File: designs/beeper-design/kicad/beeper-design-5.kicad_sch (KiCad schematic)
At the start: 7 parts, among them U12 DRV2605YZFR

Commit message: new export
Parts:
- removed C47: 2.2u, beeper-design:Pkg0201_11, symbol C335106_9
- removed C48: 2.2u, beeper-design:Pkg0201_24, symbol C335106_17
- removed R16, R17: 8K2, beeper-design:Pkg0201_39, symbol my_resistor_9
- added C47: 2.2u, beeper-design:Pkg0201_4, symbol C335106_2
- added C48: 2.2u, beeper-design:Pkg0201_16, symbol C335106_10
- added R16, R17: 8K2, beeper-design:Pkg0201_31, symbol my_resistor_8
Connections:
- net GND: now also C47.1, C48.1
- net VDDSYS: now also C48.2, R16.2, R17.2
- net mcu_hap-i2c_scl: now also R17.1
- net mcu_hap-i2c_sda: now also R16.1
- net at U12.A2 (REG): now also C47.2

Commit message: reasonble export
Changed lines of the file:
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@@
   (wire (pts (xy 248.92 113.03) (xy 248.92 111.76)) (stroke (width 0.127) (type default) (color 0 0 0 0)))
   (wire (pts (xy 228.6 121.92) (xy 233.68 121.92)) (stroke (width 0.127) (type default) (color 0 0 0 0)))
-  (wire (pts (xy 229.87 121.92) (xy 229.87 119.38)) (stroke (width 0.127) (type default) (color 0 0 0 0)))
+  (wire (pts (xy 231.14 121.92) (xy 231.14 120.65)) (stroke (width 0.127) (type default) (color 0 0 0 0)))
   (wire (pts (xy 264.16 116.84) (xy 264.16 115.57)) (stroke (width 0.127) (type default) (color 0 0 0 0)))
   (wire (pts (xy 247.65 139.7) (xy 247.65 138.43)) (stroke (width 0.127) (type default) (color 0 0 0 0)))
@@
 (junction (at 181.61 127.0) (diameter 0.762) (color 0 0 0 0 ))
 (junction (at 213.36 124.46) (diameter 0.762) (color 0 0 0 0 ))
-(junction (at 229.87 121.92) (diameter 0.762) (color 0 0 0 0 ))
+(junction (at 231.14 121.92) (diameter 0.762) (color 0 0 0 0 ))
   (label "board-io_hapdrv" (at 151.13 100.33 0)
     (effects (font (size 0.762 0.762)) (justify left bottom ))
@@
     (effects (font (size 0.762 0.762)) (justify left ))
   )
-  (global_label "mcu_hap-gpio0_gpio" (shape passive) (at 229.87 119.38 90)
+  (global_label "mcu_hap-gpio0_gpio" (shape passive) (at 231.14 120.65 90)
     (effects (font (size 0.762 0.762)) (justify left ))
   )
@@
     (instances
       (project "beeper-design"
-        (path "/219df102-d28d-b743-245e-efc9439ef913"
+        (path "/de0561a0-459a-4fb5-54e5-6d5ccc441e19"
           (reference "C48") (unit 1)
         )
@@
     (instances
       (project "beeper-design"
-        (path "/219df102-d28d-b743-245e-efc9439ef913"
+        (path "/de0561a0-459a-4fb5-54e5-6d5ccc441e19"
           (reference "R16") (unit 1)
         )
@@
     (instances
       (project "beeper-design"
-        (path "/219df102-d28d-b743-245e-efc9439ef913"
+        (path "/de0561a0-459a-4fb5-54e5-6d5ccc441e19"
           (reference "TP2") (unit 1)
         )
@@
     (instances
       (project "beeper-design"
-        (path "/219df102-d28d-b743-245e-efc9439ef913"
+        (path "/de0561a0-459a-4fb5-54e5-6d5ccc441e19"
           (reference "TP1") (unit 1)
         )
@@
     (instances
       (project "beeper-design"
-        (path "/219df102-d28d-b743-245e-efc9439ef913"
+        (path "/de0561a0-459a-4fb5-54e5-6d5ccc441e19"
           (reference "R17") (unit 1)
         )
@@
     (instances
       (project "beeper-design"
-        (path "/219df102-d28d-b743-245e-efc9439ef913"
+        (path "/de0561a0-459a-4fb5-54e5-6d5ccc441e19"
           (reference "U12") (unit 1)
         )
@@
     (instances
       (project "beeper-design"
-        (path "/219df102-d28d-b743-245e-efc9439ef913"
+        (path "/de0561a0-459a-4fb5-54e5-6d5ccc441e19"
           (reference "C47") (unit 1)
         )
@@
     (instances
       (project "beeper-design"
-        (path "/219df102-d28d-b743-245e-efc9439ef913"
+        (path "/de0561a0-459a-4fb5-54e5-6d5ccc441e19"
           (reference "#PWR?") (unit 1)
         )
@@
     (instances
       (project "beeper-design"
-        (path "/219df102-d28d-b743-245e-efc9439ef913"
+        (path "/de0561a0-459a-4fb5-54e5-6d5ccc441e19"
           (reference "#PWR?") (unit 1)
         )
@@
     (instances
       (project "beeper-design"
-        (path "/219df102-d28d-b743-245e-efc9439ef913"
+        (path "/de0561a0-459a-4fb5-54e5-6d5ccc441e19"
           (reference "#PWR?") (unit 1)
         )
@@
     (instances
       (project "beeper-design"
-        (path "/219df102-d28d-b743-245e-efc9439ef913"
+        (path "/de0561a0-459a-4fb5-54e5-6d5ccc441e19"
           (reference "#PWR?") (unit 1)
         )
@@
     (instances
       (project "beeper-design"
-        (path "/219df102-d28d-b743-245e-efc9439ef913"
+        (path "/de0561a0-459a-4fb5-54e5-6d5ccc441e19"
           (reference "#PWR?") (unit 1)
         )
@@
     (instances
       (project "beeper-design"
-        (path "/219df102-d28d-b743-245e-efc9439ef913"
+        (path "/de0561a0-459a-4fb5-54e5-6d5ccc441e19"
           (reference "#PWR?") (unit 1)
         )
@@
     (instances
       (project "beeper-design"
-        (path "/219df102-d28d-b743-245e-efc9439ef913"
-          (reference "#PWR?") (unit 1)
-        )
+        (path "/de0561a0-459a-4fb5-54e5-6d5ccc441e19"
+          (reference "#PWR?") (unit 1)
+        )

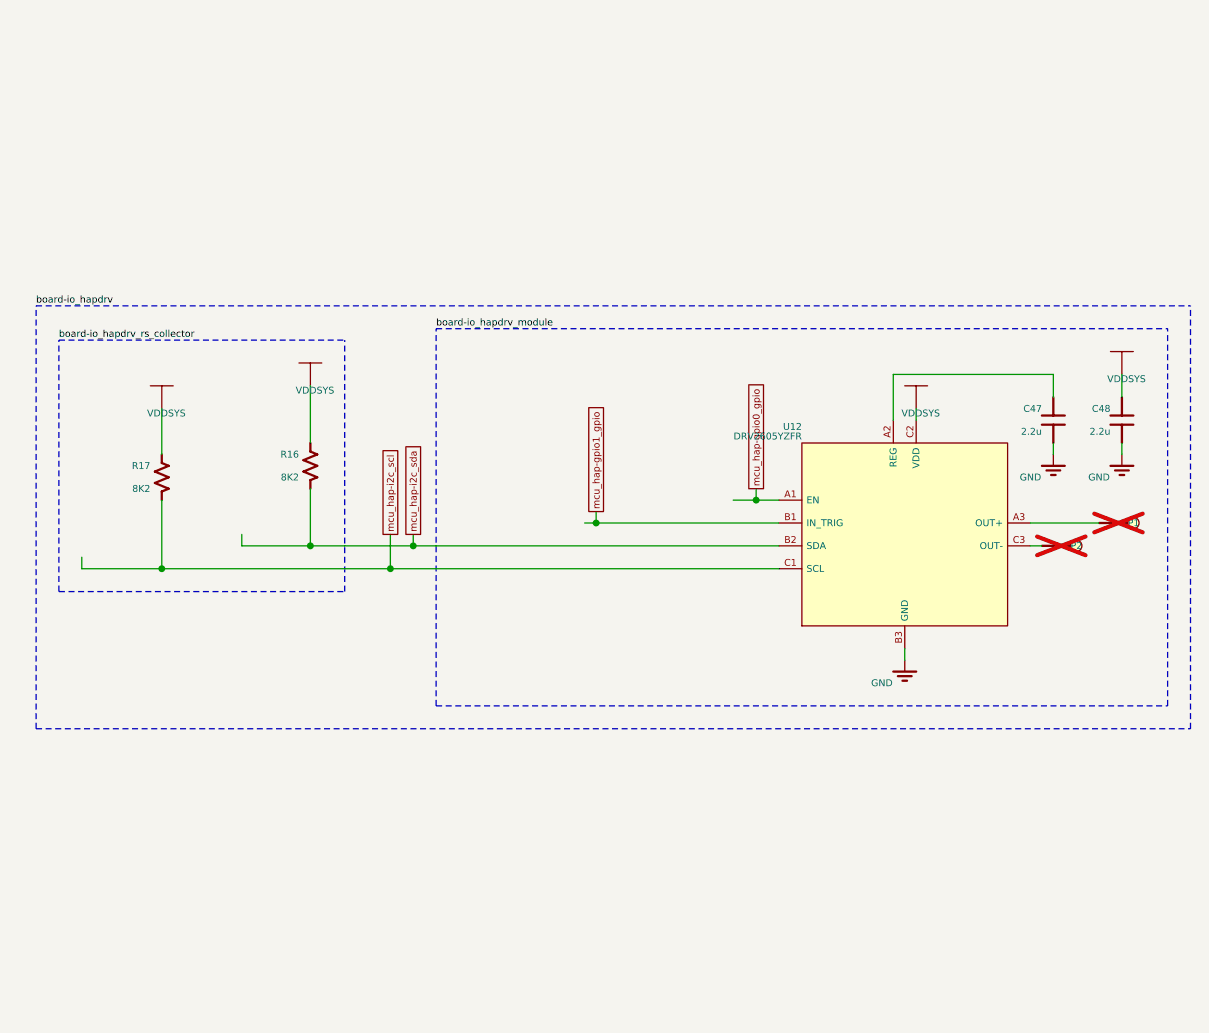
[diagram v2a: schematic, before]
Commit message: exported, yet XTALM32p keeps disappearing
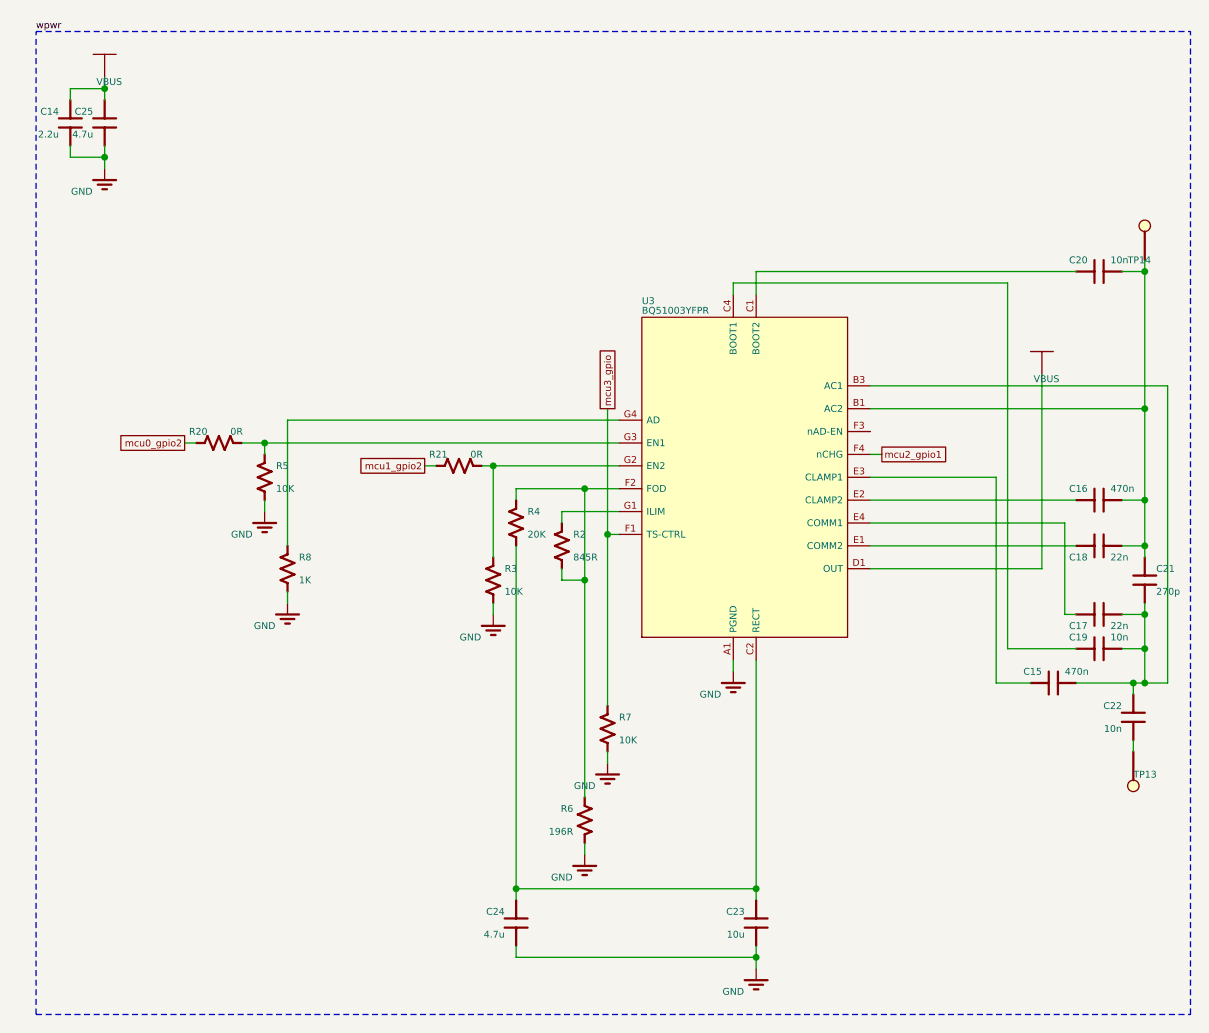
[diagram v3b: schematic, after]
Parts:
- removed C47: 2.2u, beeper-design:Pkg0201_4, symbol C335106_2
- removed C48: 2.2u, beeper-design:Pkg0201_16, symbol C335106_10
- removed R16, R17: 8K2, beeper-design:Pkg0201_31, symbol my_resistor_8
- removed TP1, TP2: (no value), beeper-design:SMD_TESTPT, symbol smd_testpoint_cmp
- removed U12: DRV2605YZFR, beeper-design:LP_7, symbol DRV2605YZFR
- added C14: 2.2u, beeper-design:Pkg0201_20, symbol C335106
- added C15: 470n, beeper-design:Pkg0201_23, symbol my_capacitor_12
- added C16: 470n, beeper-design:Pkg0201_30, symbol my_capacitor_16
- added C17: 22n, beeper-design:Pkg0201_36, symbol C505472
- added C18: 22n, beeper-design:Pkg0201_44, symbol C505472_1
- added C19: 10n, beeper-design:Pkg0201_2, symbol my_capacitor_2
- added C20: 10n, beeper-design:Pkg0201_11, symbol my_capacitor_6
- added C21: 270p, beeper-design:Pkg0201_17, symbol my_capacitor_9
- added C22: 10n, beeper-design:Pkg0201_22, symbol my_capacitor_11
- added C23: 10u, beeper-design:Pkg0402_4, symbol C105225_3
- added C24: 4.7u, beeper-design:Pkg0402_7, symbol C23733
- added C25: 4.7u, beeper-design:Pkg0402_8, symbol C23733_1
- added R2: 845R, beeper-design:Pkg0201_25, symbol my_resistor_10
- added R20: 0R, beeper-design:Pkg0201, symbol my_resistor
- added R21: 0R, beeper-design:Pkg0201_8, symbol my_resistor_3
- added R3: 10K, beeper-design:Pkg0201_4, symbol my_resistor_2
- added R4: 20K, beeper-design:Pkg0201_37, symbol my_resistor_12
- added R5: 10K, beeper-design:Pkg0201_45, symbol my_resistor_15
- added R6: 196R, beeper-design:Pkg0201_32, symbol C138167
- added R7: 10K, beeper-design:Pkg0201_12, symbol my_resistor_6
- added R8: 1K, beeper-design:Pkg0201_16, symbol my_resistor_8
- added TP13, TP14: (no value), beeper-design:SMD_TESTPT, symbol smd_testpoint_cmp
- added U3: BQ51003YFPR, beeper-design:LP_6, symbol BQ51003YFPR
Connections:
- net GND: now also C14.1, C23.1, C24.1, C25.1, R3.2, R5.2, R6.2, R7.2, R8.2, U3.A1 (PGND), U3.A2 (PGND), U3.A3 (PGND), U3.A4 (PGND)
- new net: C15.1, C17.1, C19.1, C21.2, C22.2, U3.B3 (AC1), U3.B4 (AC1)
- new net: C15.2, U3.E3 (CLAMP1)
- new net: R21.1, R3.1, U3.G2 (EN2)
- new net: R2.2, R4.1, R6.1, U3.F2 (FOD)
- new net: C23.2, C24.2, R4.2, U3.C2 (RECT), U3.C3 (RECT)
- new net: C16.1, C18.1, C20.1, C21.1, TP14.p, U3.B1 (AC2), U3.B2 (AC2)
- new net: C20.2, U3.C1 (BOOT2)
- new net: C19.2, U3.C4 (BOOT1)
- new net: C16.2, U3.E2 (CLAMP2)
- new net: C17.2, U3.E4 (COMM1)
- new net: R20.1, R5.1, U3.G3 (EN1)
- new net: C18.2, U3.E1 (COMM2)
- new net: R2.1, U3.G1 (ILIM)
- new net: R8.1, U3.G4 (AD)
- new net: C22.1, TP13.p
- new net VBUS: C14.2, C25.2, U3.D1 (OUT), U3.D2 (OUT), U3.D3 (OUT), U3.D4 (OUT)
- new net mcu0_gpio2: R20.2
- new net mcu1_gpio2: R21.2
- new net mcu2_gpio1: U3.F4 (nCHG)
- new net mcu3_gpio: R7.1, U3.F1 (TS-CTRL)

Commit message: fixed up pours, keepout regions
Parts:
- removed C15: 470n, beeper-design:Pkg0201_23, symbol my_capacitor_12
- removed C16: 470n, beeper-design:Pkg0201_30, symbol my_capacitor_16
- removed C19: 10n, beeper-design:Pkg0201_2, symbol my_capacitor_2
- removed C20: 10n, beeper-design:Pkg0201_11, symbol my_capacitor_6
- removed C21: 270p, beeper-design:Pkg0201_17, symbol my_capacitor_9
- removed C22: 10n, beeper-design:Pkg0201_22, symbol my_capacitor_11
- removed C24: 4.7u, beeper-design:Pkg0402_7, symbol C23733
- removed C25: 4.7u, beeper-design:Pkg0402_8, symbol C23733_1
- removed R2: 845R, beeper-design:Pkg0201_25, symbol my_resistor_10
- removed R20: 0R, beeper-design:Pkg0201, symbol my_resistor
- removed R21: 0R, beeper-design:Pkg0201_8, symbol my_resistor_3
- removed R3: 10K, beeper-design:Pkg0201_4, symbol my_resistor_2
- removed R4: 20K, beeper-design:Pkg0201_37, symbol my_resistor_12
- removed R5: 10K, beeper-design:Pkg0201_45, symbol my_resistor_15
- removed R7: 10K, beeper-design:Pkg0201_12, symbol my_resistor_6
- removed R8: 1K, beeper-design:Pkg0201_16, symbol my_resistor_8
- added C15: 470n, beeper-design:Pkg0201_37, symbol my_capacitor_18
- added C16: 470n, beeper-design:Pkg0201_44, symbol my_capacitor_22
- added C19: 10n, beeper-design:Pkg0201_16, symbol my_capacitor_8
- added C20: 10n, beeper-design:Pkg0201_25, symbol my_capacitor_12
- added C21: 270p, beeper-design:Pkg0201_31, symbol my_capacitor_15
- added C22: 10n, beeper-design:Pkg0201_36, symbol my_capacitor_17
- added C24: 4.7u, beeper-design:Pkg0402, symbol C23733_1
- added C25: 4.7u, beeper-design:Pkg0402_1, symbol C23733
- added R2: 845R, beeper-design:Pkg0201_39, symbol my_resistor_15
- added R20: 0R, beeper-design:Pkg0201_14, symbol my_resistor_5
- added R21: 0R, beeper-design:Pkg0201_22, symbol my_resistor_8
- added R3: 10K, beeper-design:Pkg0201_18, symbol my_resistor_7
- added R4: 20K, beeper-design:Pkg0201_3, symbol my_resistor
- added R5: 10K, beeper-design:Pkg0201_11, symbol my_resistor_3
- added R7: 10K, beeper-design:Pkg0201_26, symbol my_resistor_11
- added R8: 1K, beeper-design:Pkg0201_30, symbol my_resistor_13
- C14: footprint beeper-design:Pkg0201_20 -> beeper-design:Pkg0201_34
- C17: footprint beeper-design:Pkg0201_36 -> beeper-design:Pkg0201_2
- C18: footprint beeper-design:Pkg0201_44 -> beeper-design:Pkg0201_10
- C23: footprint beeper-design:Pkg0402_4 -> beeper-design:Pkg0402_6
- R6: footprint beeper-design:Pkg0201_32 -> beeper-design:Pkg0201_46
- U3: footprint beeper-design:LP_6 -> beeper-design:LP_1
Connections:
- net GND: now also C24.1, C25.1, R3.2, R5.2, R7.2, R8.2
- net VBUS: now also C25.2
- net mcu0_gpio2: now also R20.2
- net mcu1_gpio2: now also R21.2
- net mcu3_gpio: now also R7.1
- net at C17.1, U3.B3 (AC1), U3.B4 (AC1): now also C15.1, C19.1, C21.2, C22.2
- net at U3.E3 (CLAMP1): now also C15.2
- net at U3.G2 (EN2): now also R21.1, R3.1
- net at R6.1, U3.F2 (FOD): now also R2.2, R4.1
- net at C23.2, U3.C2 (RECT), U3.C3 (RECT): now also C24.2, R4.2
- net at C18.1, TP14.p, U3.B1 (AC2)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: now also C16.1, C20.1, C21.1
- net at U3.C1 (BOOT2): now also C20.2
- net at U3.C4 (BOOT1): now also C19.2
- net at U3.E2 (CLAMP2): now also C16.2
- net at U3.G3 (EN1): now also R20.1, R5.1
- net at U3.G1 (ILIM): now also R2.1
- net at U3.G4 (AD): now also R8.1
- net at TP13.p: now also C22.1

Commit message: exported to Kicad, fixed Kicad, exported gerbers
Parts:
- removed C14: 2.2u, beeper-design:Pkg0201_34, symbol C335106
- removed C15: 470n, beeper-design:Pkg0201_37, symbol my_capacitor_18
- removed C16: 470n, beeper-design:Pkg0201_44, symbol my_capacitor_22
- removed C19: 10n, beeper-design:Pkg0201_16, symbol my_capacitor_8
- removed C20: 10n, beeper-design:Pkg0201_25, symbol my_capacitor_12
- removed C21: 270p, beeper-design:Pkg0201_31, symbol my_capacitor_15
- removed C22: 10n, beeper-design:Pkg0201_36, symbol my_capacitor_17
- removed C23: 10u, beeper-design:Pkg0402_6, symbol C105225_3
- removed C24: 4.7u, beeper-design:Pkg0402, symbol C23733_1
- removed C25: 4.7u, beeper-design:Pkg0402_1, symbol C23733
- removed R2: 845R, beeper-design:Pkg0201_39, symbol my_resistor_15
- removed R20: 0R, beeper-design:Pkg0201_14, symbol my_resistor_5
- removed R21: 0R, beeper-design:Pkg0201_22, symbol my_resistor_8
- removed R3: 10K, beeper-design:Pkg0201_18, symbol my_resistor_7
- removed R4: 20K, beeper-design:Pkg0201_3, symbol my_resistor
- removed R5: 10K, beeper-design:Pkg0201_11, symbol my_resistor_3
- removed R7: 10K, beeper-design:Pkg0201_26, symbol my_resistor_11
- removed R8: 1K, beeper-design:Pkg0201_30, symbol my_resistor_13
- added C14: 2.2u, beeper-design:Pkg0201_1, symbol C335106_1
- added C15: 470n, beeper-design:Pkg0201_4, symbol my_capacitor_1
- added C16: 470n, beeper-design:Pkg0201_11, symbol my_capacitor_5
- added C19: 10n, beeper-design:Pkg0201_31, symbol my_capacitor_18
- added C20: 10n, beeper-design:Pkg0201_40, symbol my_capacitor_22
- added C21: 270p, beeper-design:Pkg0201_46, symbol my_capacitor_25
- added C22: 10n, beeper-design:Pkg0201_3, symbol my_capacitor
- added C23: 10u, beeper-design:Pkg0402_2, symbol C105225_1
- added C24: 4.7u, beeper-design:Pkg0402_5, symbol C23733
- added C25: 4.7u, beeper-design:Pkg0402_6, symbol C23733_1
- added R2: 845R, beeper-design:Pkg0201_6, symbol my_resistor
- added R20: 0R, beeper-design:Pkg0201_29, symbol my_resistor_7
- added R21: 0R, beeper-design:Pkg0201_37, symbol my_resistor_10
- added R3: 10K, beeper-design:Pkg0201_33, symbol my_resistor_9
- added R4: 20K, beeper-design:Pkg0201_18, symbol my_resistor_2
- added R5: 10K, beeper-design:Pkg0201_26, symbol my_resistor_5
- added R7: 10K, beeper-design:Pkg0201_41, symbol my_resistor_13
- added R8: 1K, beeper-design:Pkg0201_45, symbol my_resistor_15
- C17: footprint beeper-design:Pkg0201_2 -> beeper-design:Pkg0201_17
- C18: footprint beeper-design:Pkg0201_10 -> beeper-design:Pkg0201_25
- R6: footprint beeper-design:Pkg0201_46 -> beeper-design:Pkg0201_13
- U3: footprint beeper-design:LP_1 -> beeper-design:LP_6
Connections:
- net GND: now also C14.1, C23.1, C24.1, C25.1, R3.2, R5.2, R7.2, R8.2
- net VBUS: now also C14.2, C25.2
- net mcu0_gpio2: now also R20.2
- net mcu1_gpio2: now also R21.2
- net mcu3_gpio: now also R7.1
- net at C18.1, TP14.p, U3.B1 (AC2)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: now also C16.1, C20.1, C21.1
- net at U3.G1 (ILIM): now also R2.1
- net at R6.1, U3.F2 (FOD): now also R2.2, R4.1
- net at U3.C2 (RECT), U3.C3 (RECT): now also C23.2, C24.2, R4.2
- net at U3.G3 (EN1): now also R20.1, R5.1
- net at C17.1, U3.B3 (AC1), U3.B4 (AC1): now also C15.1, C19.1, C21.2, C22.2
- net at U3.C1 (BOOT2): now also C20.2
- net at U3.C4 (BOOT1): now also C19.2
- net at U3.E2 (CLAMP2): now also C16.2
- net at U3.E3 (CLAMP1): now also C15.2
- net at U3.G2 (EN2): now also R21.1, R3.1
- net at U3.G4 (AD): now also R8.1
- net at TP13.p: now also C22.1
